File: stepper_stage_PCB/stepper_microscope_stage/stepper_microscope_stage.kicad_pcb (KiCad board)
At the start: 2 copper layers, 131.5 x 163.5 mm, 22 parts, among them J1 Conn_01x04_Socket

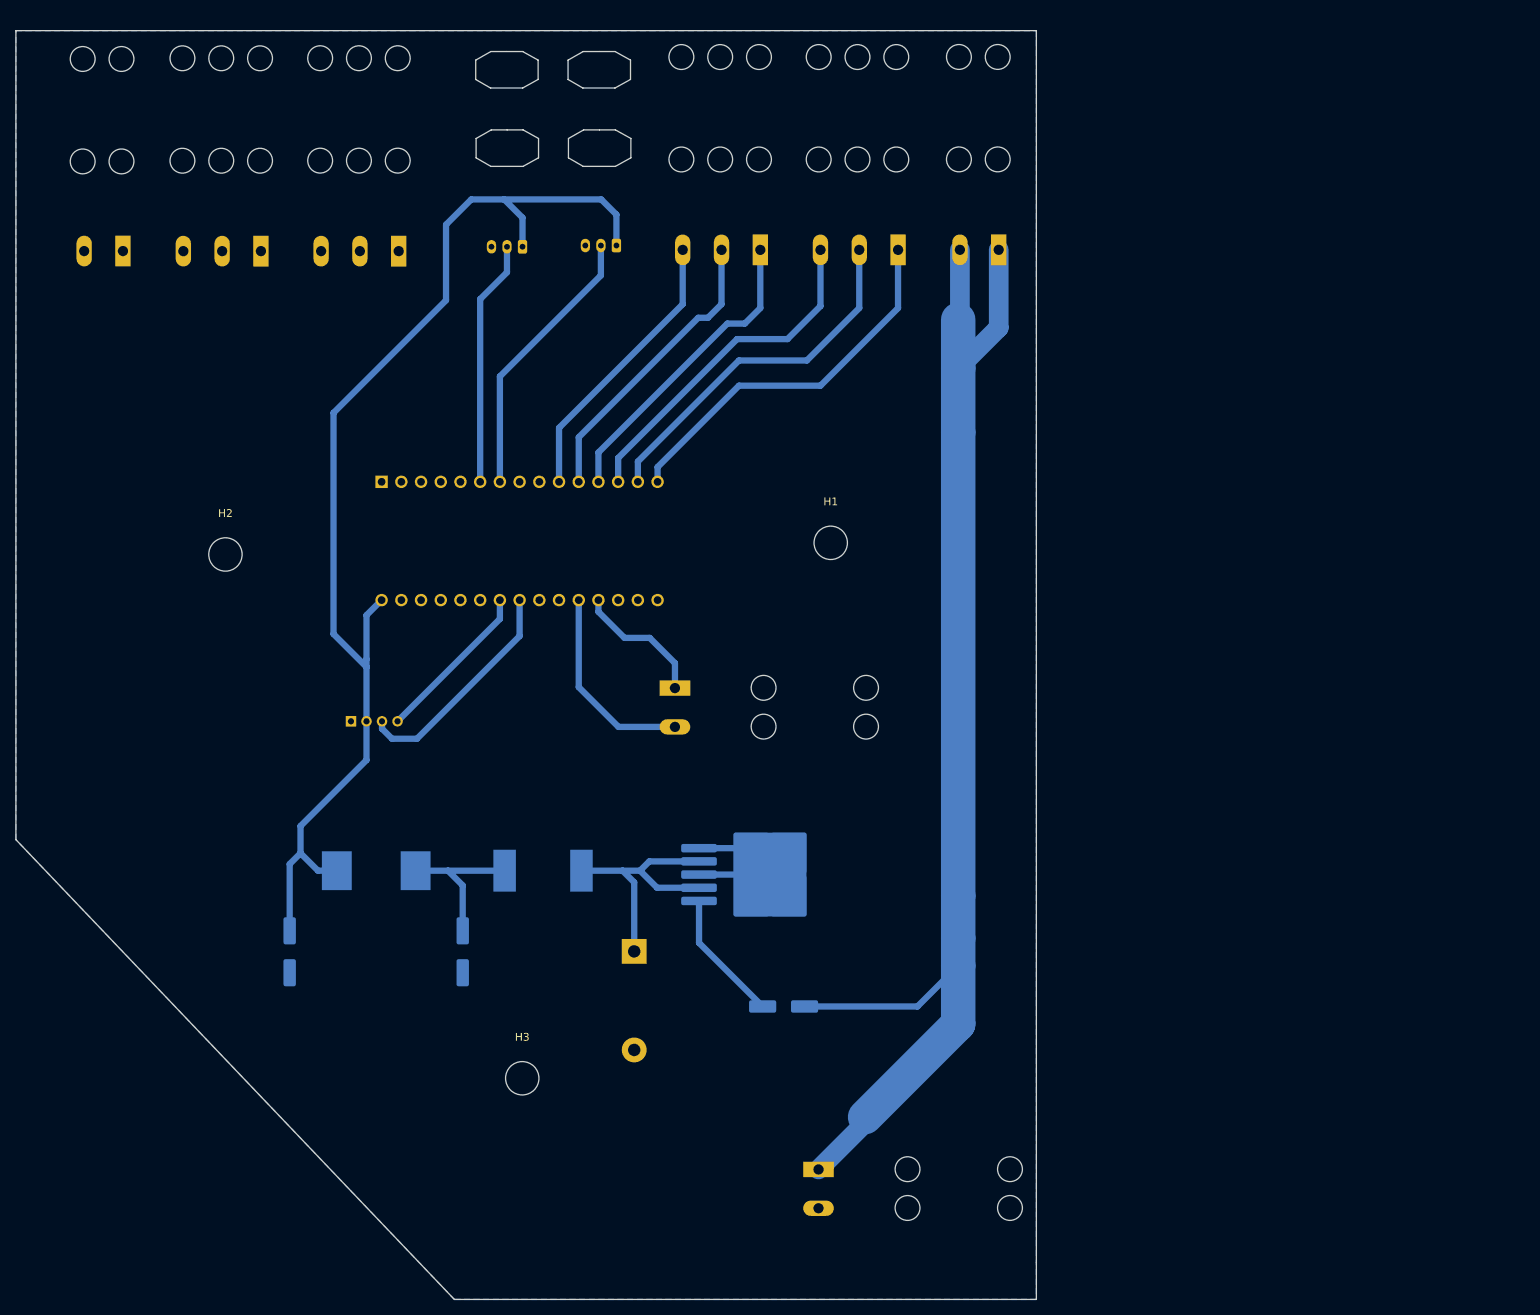
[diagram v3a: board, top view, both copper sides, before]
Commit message: Routed and filled board. Missing switch
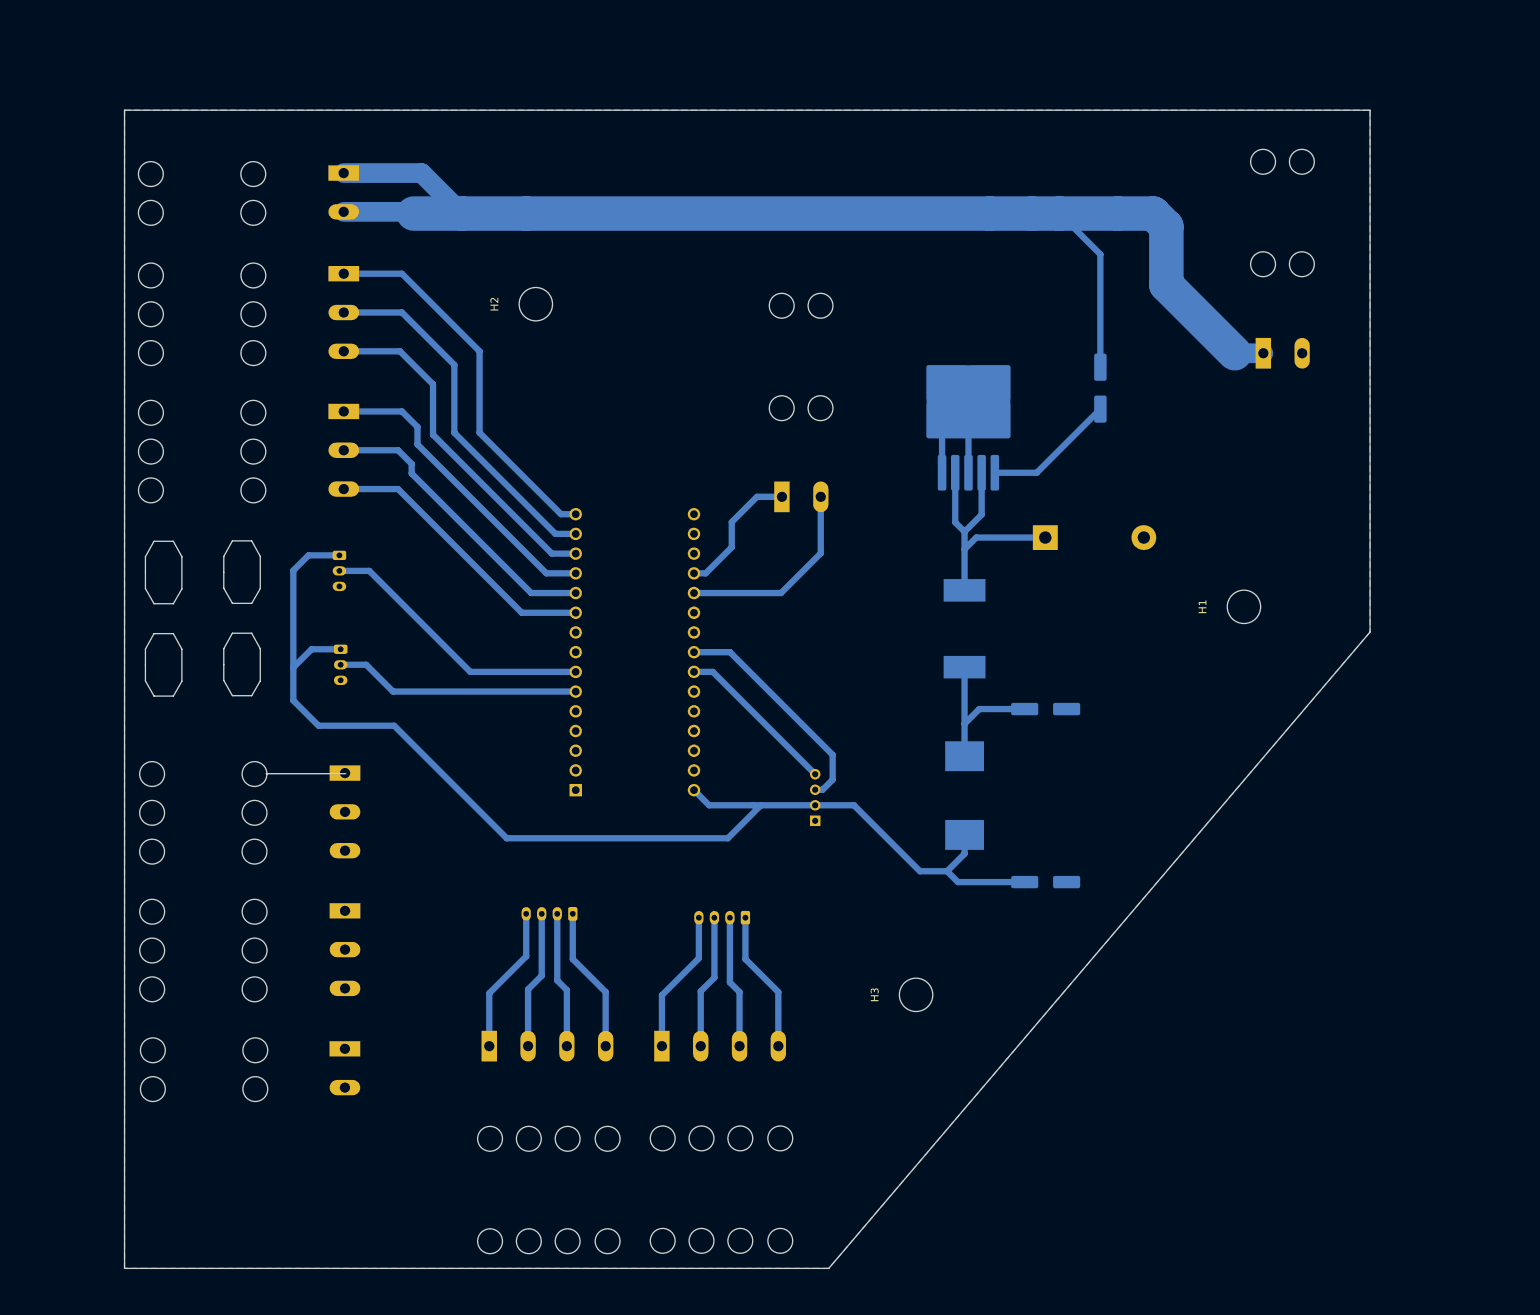
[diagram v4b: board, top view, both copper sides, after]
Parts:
- added J2: Screw_Terminal_01x04, TerminalBlock:TerminalBlock_Altech_AK300-4_P5.00mm, B.Cu at (110.8, 147.9)
- added J3: Screw_Terminal_01x04, TerminalBlock:TerminalBlock_Altech_AK300-4_P5.00mm, B.Cu at (88.5, 147.9)
- added J4: Conn_01x04_Socket, Connector_JST:JST_PH_B4B-PH-K_1x04_P2.00mm_Vertical, B.Cu at (121.5, 131.3)
- added J5: Conn_01x04_Socket, Connector_JST:JST_PH_B4B-PH-K_1x04_P2.00mm_Vertical, B.Cu at (99.3, 130.8)
- moved VIN1 119.8 mm to (188.2, 58.6), turned to 0 degrees
- moved STEPGND1 106.7 mm to (69.9, 148.2), turned to -90 degrees
- moved C3 97.8 mm to (160.2, 126.7), turned to 0 degrees
- moved C1 89.5 mm to (167.2, 63.1), turned to -90 degrees
- moved STEPSIGGND2 85.7 mm to (69.9, 130.4), turned to -90 degrees
- moved STEPPWR1 85.0 mm to (69.7, 35.4), turned to -90 degrees
- moved C2 81.4 mm to (160.2, 104.4), turned to 0 degrees
- moved L2 76.4 mm to (149.8, 115.6), turned to -90 degrees
- moved D1 75.2 mm to (160.2, 82.3), turned to 0 degrees
- moved STEPSIG1 71.5 mm to (69.8, 48.3), turned to -90 degrees
- moved STEPSIGGND1 67.6 mm to (69.9, 112.7), turned to -90 degrees
- moved TL2575 65.3 mm to (150.2, 66.3), turned to 90 degrees
- moved L1 62.6 mm to (149.8, 94.1), turned to -90 degrees
- moved J1 61.2 mm to (130.5, 118.8), turned to 0 degrees
- moved STEPSIG2 57.6 mm to (69.8, 66.1), turned to -90 degrees
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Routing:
- net Net-(J3-Pin_1): track 0.00 -> 19.0 mm
- net Net-(J3-Pin_4): track 0.00 -> 18.8 mm
- net Net-(J2-Pin_1): track 0.00 -> 18.5 mm
- net Net-(J2-Pin_4): track 0.00 -> 18.3 mm
- net Net-(J3-Pin_2): track 0.00 -> 17.8 mm
- net Net-(J3-Pin_3): track 0.00 -> 17.6 mm
- net Net-(J2-Pin_2): track 0.00 -> 17.3 mm
- net Net-(J2-Pin_3): track 0.00 -> 17.1 mm
- net +24V: track 166.2 -> 169.9 mm
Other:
- board size 131.5 x 163.5 mm -> 160.5 x 149.2 mm

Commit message: Version 1 acheived!
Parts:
- added SW1: SW_SPDT, Custom_switches:spdt_4mm_pitch_with_tension_relief, F.Cu at (172.5, 41.5)
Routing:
- net +24V: track 169.9 -> 168.4 mm
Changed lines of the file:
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@@
   (net 41 "Net-(J3-Pin_3)")
   (net 42 "Net-(J3-Pin_4)")
+  (net 43 "unconnected-(SW1-C-Pad3)")
   (footprint "MountingHole:MountingHole_4.3mm_M4" (layer "F.Cu")
     (at 185.75 91.25 90)
@@
     (pad "" np_thru_hole circle (at 0 0 90) (size 4.3 4.3) (drill 4.3) (layers "*.Cu" "*.Mask"))
   )
+  (footprint "Custom_switches:spdt_4mm_pitch_with_tension_relief" (layer "F.Cu")
+    (at 172.5 41.5 90)
+    (property "Sheetfile" "stepper_microscope_stage.kicad_sch")
+    (property "Sheetname" "")
+    (property "ki_description" "Switch, single pole double throw")
+    (property "ki_keywords" "switch single-pole double-throw spdt ON-ON")
+    (attr through_hole)
+    (fp_text reference "SW1" (at 0 3.6875 90) (layer "F.SilkS")
+        (effects (font (size 1 1) (thickness 0.15)))
+    )
+    (fp_text value "SW_SPDT" (at 0 -3.6875 90) (layer "F.Fab")
+        (effects (font (size 1 1) (thickness 0.15)))
+    )
+    (fp_line (start -10.2362 0) (end -10.2362 2.667)
+      (stroke (width 0.1) (type default)) (layer "F.SilkS"))
+    (fp_line (start -5.8166 -2.667) (end -5.8166 2.667)
+      (stroke (width 0.1) (type default)) (layer "F.SilkS"))
+    (fp_line (start -2.0066 2.667) (end -2.0066 -2.667)
+      (stroke (width 0.1) (type default)) (layer "F.SilkS"))
+    (fp_line (start 10.2362 0) (end 10.2362 -2.667)
+      (stroke (width 0.1) (type default)) (layer "F.SilkS"))
+    (fp_rect (start -10.2362 2.667) (end 10.2362 -2.667)
+      (stroke (width 0.1) (type default)) (fill none) (layer "F.SilkS"))
+    (fp_line (start -10.0076 2.4384) (end -10.0076 -2.4384)
+      (stroke (width 0.05) (type default)) (layer "F.CrtYd"))
+    (fp_line (start -5.56 -2.44) (end -10.0076 -2.4384)
+      (stroke (width 0.05) (type default)) (layer "F.CrtYd"))
+    (fp_line (start -5.56 -2.44) (end 5.56 -2.44)
+      (stroke (width 0.05) (type default)) (layer "F.CrtYd"))
+    (fp_line (start -5.56 2.44) (end -10.0076 2.4384)
+      (stroke (width 0.05) (type default)) (layer "F.CrtYd"))
+    (fp_line (start 5.56 -2.44) (end 10.0076 -2.4384)
+      (stroke (width 0.05) (type default)) (layer "F.CrtYd"))
+    (fp_line (start 5.56 2.44) (end -5.56 2.44)
+      (stroke (width 0.05) (type default)) (layer "F.CrtYd"))
+    (fp_line (start 5.56 2.44) (end 10.0076 2.4384)
+      (stroke (width 0.05) (type default)) (layer "F.CrtYd"))
+    (fp_line (start 10.0076 2.4384) (end 10.0076 -2.4384)
+      (stroke (width 0.05) (type default)) (layer "F.CrtYd"))
+    (pad "" np_thru_hole circle (at -8 0 90) (size 3.5 3.5) (drill 1.75) (layers "F&B.Cu" "*.Mask"))
+    (pad "" np_thru_hole circle (at 8 0 90) (size 3.5 3.5) (drill 1.75) (layers "F&B.Cu" "*.Mask"))
+    (pad "1" thru_hole oval (at -4 0 90) (size 2.625 4.375) (drill 1.75) (layers "*.Cu" "*.Mask")
+      (net 8 "+24V") (pinfunction "A") (pintype "passive") (thermal_bridge_angle 45))
+    (pad "2" thru_hole oval (at 0 0 90) (size 2.625 4.375) (drill 1.75) (layers "*.Cu" "*.Mask")
+      (net 8 "+24V") (pinfunction "B") (pintype "passive") (thermal_bridge_angle 45))
+    (pad "3" thru_hole oval (at 4 0 90) (size 2.625 4.375) (drill 1.75) (layers "*.Cu" "*.Mask")
+      (net 43 "unconnected-(SW1-C-Pad3)") (pinfunction "C") (pintype "passive+no_connect") (thermal_bridge_angle 45))
+  )
   (footprint "Capacitor_SMD:CP_Elec_6.3x7.7" (layer "B.Cu")
     (at 160.2 126.722144)
@@
   (segment (start 63.25 86.572144) (end 63.25 99.072144) (width 0.8128) (layer "B.Cu") (net 7))
   (segment (start 135.5 116.822144) (end 130.5 116.822144) (width 0.8128) (layer "B.Cu") (net 7))
-  (segment (start 188.25 58.572144) (end 184.572144 58.572144) (width 2.54) (layer "B.Cu") (net 8))
-  (segment (start 85 40.572144) (end 78.75 40.572144) (width 4.445) (layer "B.Cu") (net 8))
+  (segment (start 85 40.572144) (end 78.75 40.572144) (width 2.54) (layer "B.Cu") (net 8))
   (segment (start 79.78 35.352144) (end 85 40.572144) (width 2.54) (layer "B.Cu") (net 8))
+  (segment (start 163.177856 41.75) (end 162 40.572144) (width 0.8128) (layer "B.Cu") (net 8))
   (segment (start 167.25 45.822144) (end 162 40.572144) (width 0.8128) (layer "B.Cu") (net 8))
-  (segment (start 78.53 40.352144) (end 78.75 40.572144) (width 0.8128) (layer "B.Cu") (net 8))
-  (segment (start 175.75 49.75) (end 175.75 42.25) (width 4.445) (layer "B.Cu") (net 8))
-  (segment (start 158.45 40.572144) (end 162 40.572144) (width 4.445) (layer "B.Cu") (net 8))
-  (segment (start 93.265 40.572144) (end 153 40.572144) (width 4.445) (layer "B.Cu") (net 8))
+  (segment (start 183 51.75) (end 176.75 45.5) (width 2.54) (layer "B.Cu") (net 8))
+  (segment (start 78.53 40.352144) (end 78.75 40.572144) (width 2.54) (layer "B.Cu") (net 8))
+  (segment (start 158.45 40.572144) (end 162 40.572144) (width 2.54) (layer "B.Cu") (net 8))
+  (segment (start 93.265 40.572144) (end 153 40.572144) (width 2.54) (layer "B.Cu") (net 8))
+  (segment (start 162.927856 41.5) (end 162 40.572144) (width 2.54) (layer "B.Cu") (net 8))
   (segment (start 167.25 60.372144) (end 167.25 45.822144) (width 0.8128) (layer "B.Cu") (net 8))
   (segment (start 69.74 35.352144) (end 79.78 35.352144) (width 2.54) (layer "B.Cu") (net 8))
-  (segment (start 162 40.572144) (end 169.5 40.572144) (width 4.445) (layer "B.Cu") (net 8))
-  (segment (start 174.072144 40.572144) (end 169.5 40.572144) (width 4.445) (layer "B.Cu") (net 8))
-  (segment (start 184.572144 58.572144) (end 175.75 49.75) (width 4.445) (layer "B.Cu") (net 8))
-  (segment (start 153 40.572144) (end 158.45 40.572144) (width 4.445) (layer "B.Cu") (net 8))
+  (segment (start 153 40.572144) (end 158.45 40.572144) (width 2.54) (layer "B.Cu") (net 8))
+  (segment (start 188.25 58.572144) (end 184.822144 58.572144) (width 2.54) (layer "B.Cu") (net 8))
   (segment (start 69.74 40.352144) (end 78.53 40.352144) (width 2.54) (layer "B.Cu") (net 8))
+  (segment (start 172.5 41.5) (end 162.927856 41.5) (width 2.54) (layer "B.Cu") (net 8))
+  (segment (start 184.822144 58.572144) (end 183 56.75) (width 2.54) (layer "B.Cu") (net 8))
   (segment (start 69.765 35.602144) (end 69.75 35.617144) (width 0.8128) (layer "B.Cu") (net 8))
-  (segment (start 175.75 42.25) (end 174.072144 40.572144) (width 4.445) (layer "B.Cu") (net 8))
-  (segment (start 93.265 40.572144) (end 85 40.572144) (width 4.445) (layer "B.Cu") (net 8))
+  (segment (start 176.75 45.5) (end 172.5 45.5) (width 2.54) (layer "B.Cu") (net 8))
+  (segment (start 183 56.75) (end 183 51.75) (width 2.54) (layer "B.Cu") (net 8))
+  (segment (start 93.265 40.572144) (end 85 40.572144) (width 2.54) (layer "B.Cu") (net 8))
   (segment (start 77.25 48.322144) (end 87.25 58.322144) (width 0.8128) (layer "B.Cu") (net 21))
   (segment (start 87.25 68.822144) (end 97.74 79.312144) (width 0.8128) (layer "B.Cu") (net 21))
